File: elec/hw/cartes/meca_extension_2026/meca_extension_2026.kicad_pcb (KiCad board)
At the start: 2 copper layers, 112.5 x 54.9 mm, 168 parts, among them J1 2-1445055-3, J10 22053051, J11 22272021, J12 22272021, J13 22053051, J14 22272031, J15 22272031, J2 22272021, J20 5264-3P, J21 5264-3P, J22 5264-3P, J23 5264-3P, J24 22053031, J25 22053031, J26 22053051, J27 22053041, J28 22053031, J29 22053031, J3 22272021, J4 22053051, J5 22272021, J6 22272021, J7 22053051, J8 22272021, J9 22272021, Q1 SI2310, Q10 SI2310, Q11 SI2310, Q12 2N7002, Q19 BSS84, Q2 SI2310, Q20 2N7002, Q3 2N7002, Q4 SI2310, Q5 SI2310, Q6 2N7002, Q7 SI2310, Q8 SI2310, Q9 2N7002, U1 TCA9548APWR, U11 LV14340DDAR, U2 PCA9535PW, U3 TLA2528IRTER, U4 TLV9061IDBVR, U5 TLV9061IDBVR, U6 TLV9061IDBVR, U7 TLV9061IDBVR, U8 74HCT238PW

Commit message: meca ext : first draft of compenent placement
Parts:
- C27, C29, C30, C31, D13, J21, J22, J23, Q19, Q20, R71, R72, R73, R74, R75: moved to B.Cu
- moved C27 248.8 mm to (110.5, 102.0), turned to 90 degrees
- moved J23 240.2 mm to (59.2, 110.8), turned to 90 degrees
- moved J21 213.1 mm to (70.8, 56.1), turned to 90 degrees
- moved Q10 211.6 mm to (37.2, 103.9), turned to -90 degrees
- moved R47 207.6 mm to (37.2, 100.9), turned to 0 degrees
- moved J13 206.9 mm to (46.7, 110.8)
- moved R50 206.6 mm to (42.6, 107.8), turned to 0 degrees
- moved J22 203.4 mm to (136.5, 41.6), turned to -90 degrees
- moved R52 200.6 mm to (42.6, 105.8), turned to 0 degrees
- moved R51 200.3 mm to (46.6, 105.3), turned to -90 degrees
- moved J11 200.2 mm to (36.7, 112.9), turned to -90 degrees
- moved Q12 198.9 mm to (49.7, 105.4), turned to -90 degrees
- moved R40 192.2 mm to (161.5, 85.2), turned to 90 degrees
- moved D7 189.2 mm to (36.7, 107.4), turned to 0 degrees
- moved Q8 189.1 mm to (164.6, 85.2), turned to 0 degrees
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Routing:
- net +BATT: track 5.66 -> 22.6 mm
- net Net-(D3-A): track 0.00 -> 8.50 mm
- net Net-(D5-A): track 0.00 -> 8.50 mm
- net Net-(D7-A): track 0.00 -> 8.50 mm
- net GND: track 1.95 -> 7.78 mm
- net /solenoid_valve_cmd_1_3v3: track 0.00 -> 1.95 mm
- net /solenoid_valve_cmd_3_3v3: track 0.00 -> 1.95 mm
- net /solenoid_valve_cmd_2_3v3: track 0.00 -> 1.95 mm

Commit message: meca ext : second draft of component placement
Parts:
- C23, C24, C25, C26, R76, U1, U3: moved to B.Cu
- moved R78 242.5 mm to (118.5, 86.0), turned to -90 degrees
- moved R77 242.0 mm to (118.5, 83.0), turned to -90 degrees
- moved C13 238.9 mm to (122.5, 78.5), turned to 90 degrees
- moved R83 238.6 mm to (152.6, 90.5), turned to 0 degrees
- moved R84 234.2 mm to (152.6, 88.5), turned to 0 degrees
- moved C18 233.3 mm to (149.6, 92.0), turned to -90 degrees
- moved C25 233.1 mm to (77.0, 100.5), turned to -45 degrees
- moved C16 231.1 mm to (143.1, 81.0), turned to 90 degrees
- moved C19 230.8 mm to (147.1, 92.0), turned to -90 degrees
- moved R85 229.9 mm to (152.6, 86.5), turned to 0 degrees
- moved C17 229.3 mm to (149.6, 84.5), turned to 90 degrees
- moved R79 227.8 mm to (127.1, 76.0), turned to 0 degrees
- moved C24 227.4 mm to (143.0, 61.5), turned to 150 degrees
- moved R80 227.3 mm to (127.1, 78.0), turned to 0 degrees
- moved C15 225.8 mm to (129.6, 88.0), turned to 0 degrees
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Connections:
- net /vaccum_1/led_cmd renamed /channel_0/led_cmd
- net /vaccum_2/led_cmd renamed /channel_1/led_cmd
- net /vaccum_3/led_cmd renamed /channel_2/led_cmd
- net /vaccum_4/led_cmd renamed /channel_3/led_cmd
- R19 pad 2: Net-(U1-SC6) -> Net-(U1-SD6)
- R21 pad 2: Net-(U1-SC6) -> Net-(U1-SD7)
- R22 pad 2: Net-(U1-SC6) -> Net-(U1-SC7)
- TP1 pad 1: Net-(U1-SC6) -> Net-(U1-SD6)
- TP3 pad 1: Net-(U1-SC6) -> Net-(U1-SD7)
- TP4 pad 1: Net-(U1-SC6) -> Net-(U1-SC7)
- U1 pad 17: Net-(U1-SC6) -> Net-(U1-SD6)
- U1 pad 19: Net-(U1-SC6) -> Net-(U1-SD7)
- U1 pad 20: Net-(U1-SC6) -> Net-(U1-SC7)
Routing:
- net +BATT: track 22.6 -> 11.3 mm
- net Net-(D3-A): track 8.50 -> 0.00 mm
- net Net-(D5-A): track 8.50 -> 0.00 mm

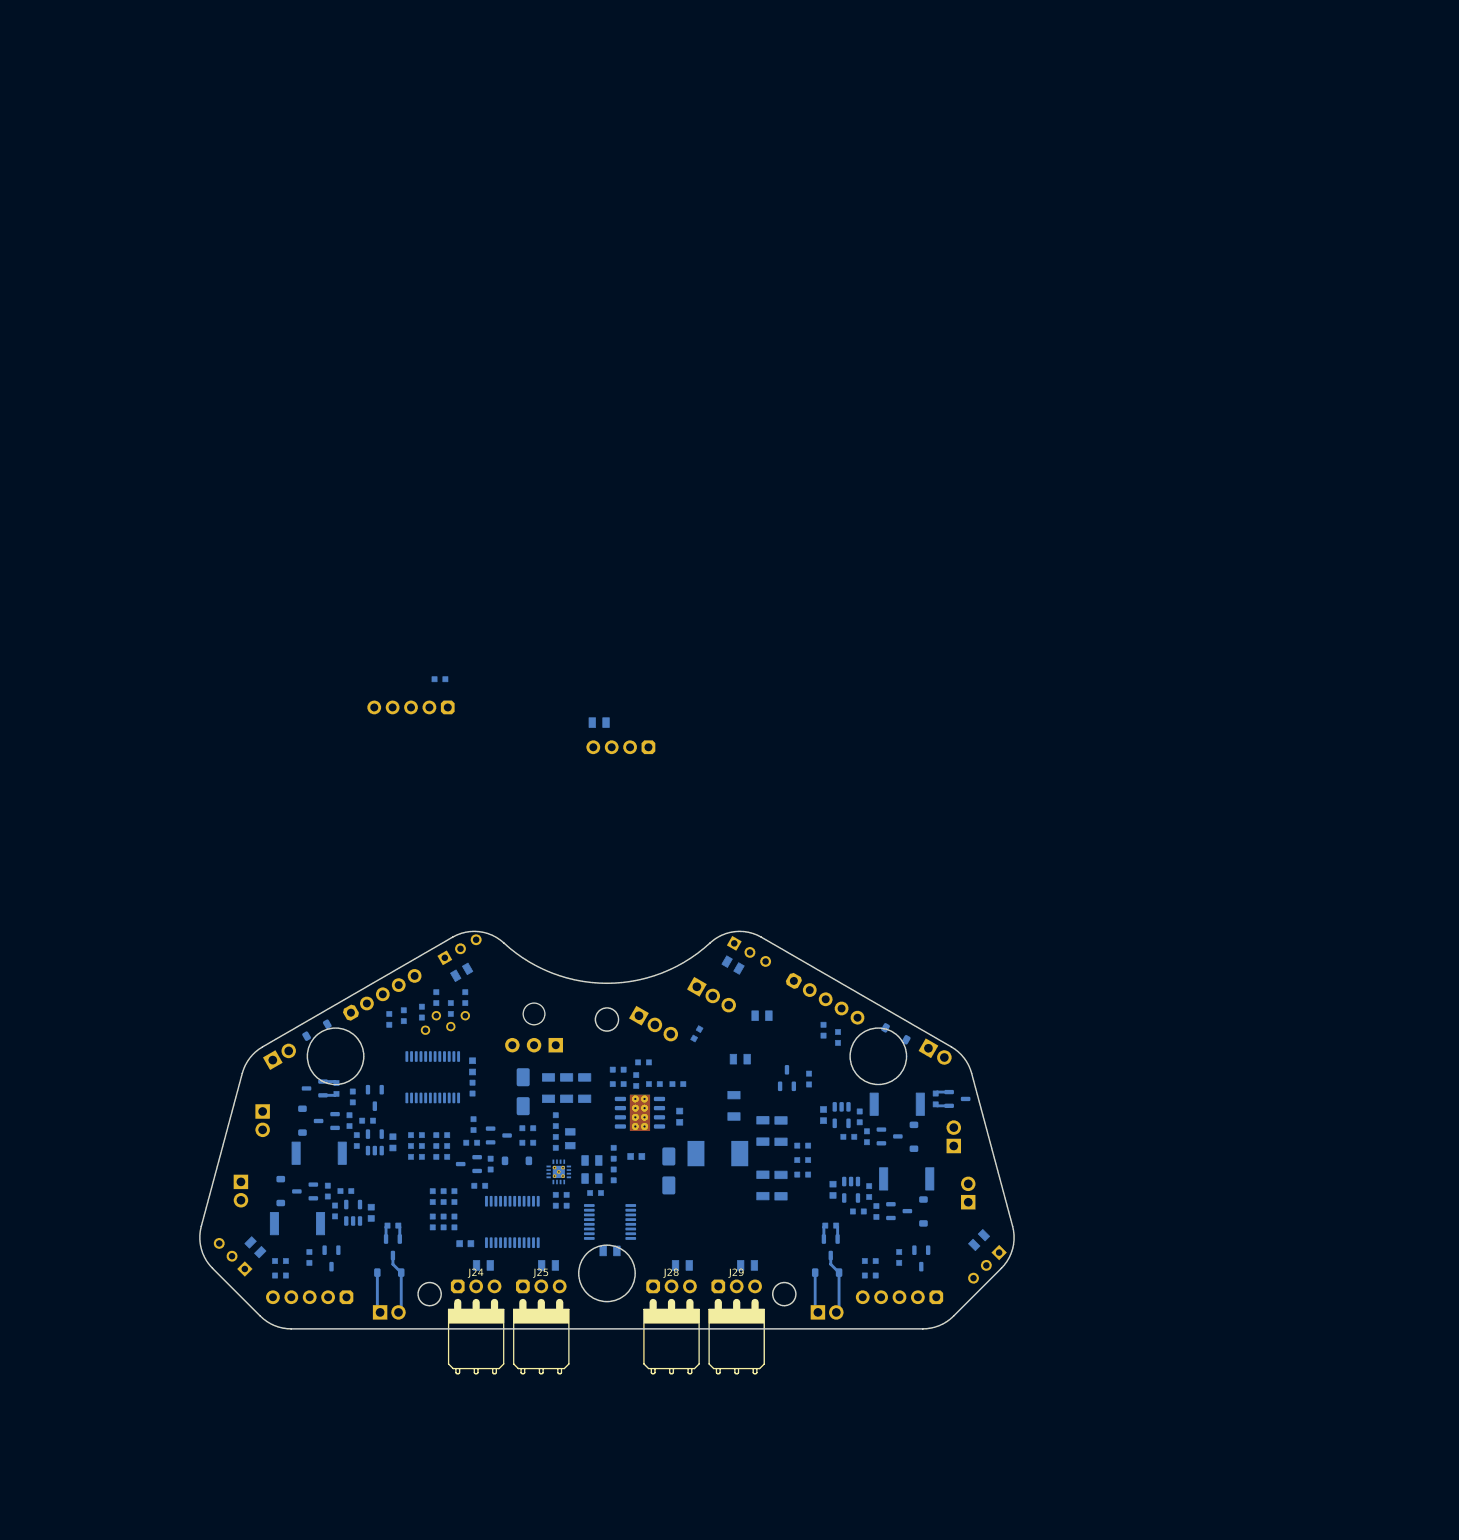
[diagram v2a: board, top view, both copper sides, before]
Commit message: meca_extension : updated board edge cut and connector placement
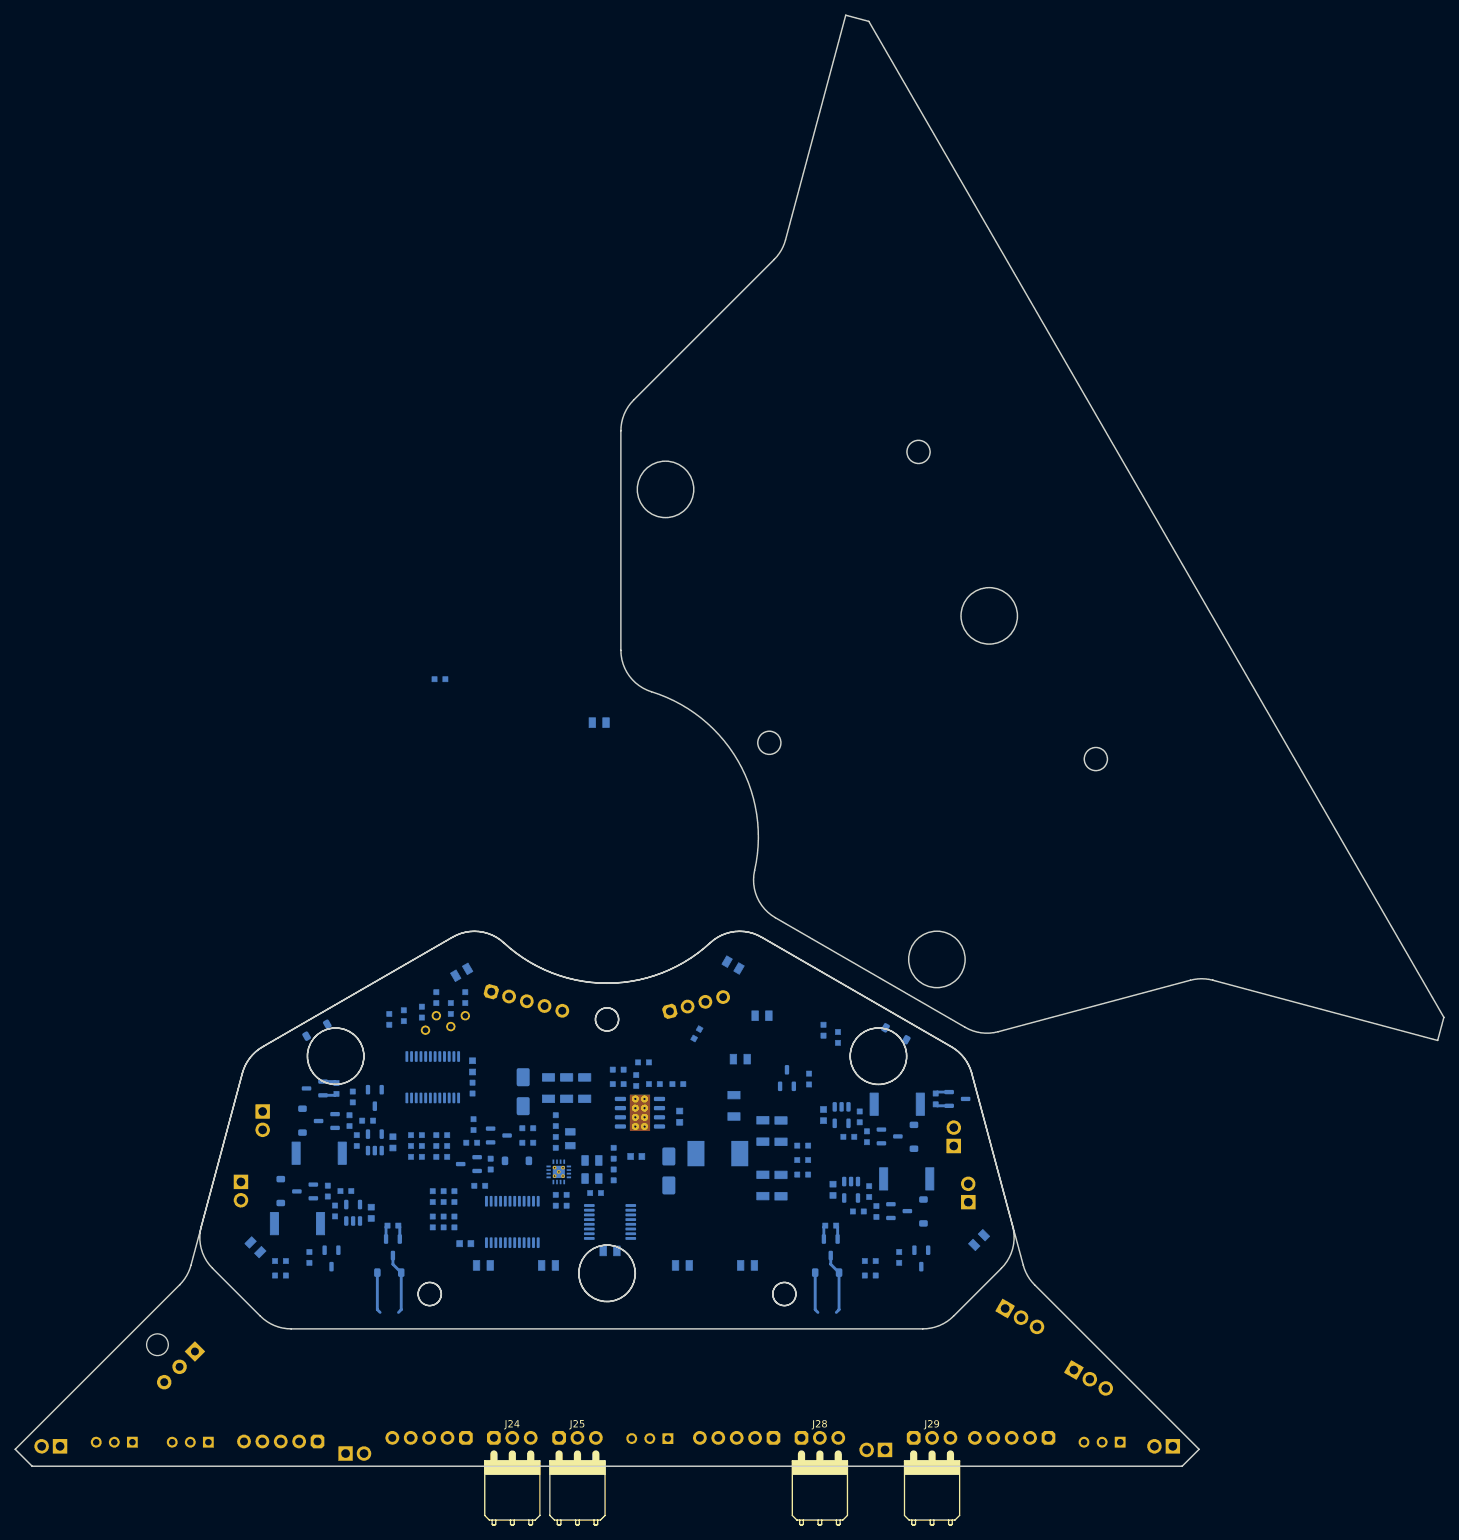
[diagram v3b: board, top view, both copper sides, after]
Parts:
- moved J22 102.8 mm to (68.0, 127.4), turned to 90 degrees
- moved J5 98.7 mm to (162.7, 128.5), turned to 90 degrees
- moved J8 97.6 mm to (90.7, 129.0), turned to -90 degrees
- moved J10 81.7 mm to (101.0, 126.8), turned to 180 degrees
- moved J7 78.4 mm to (143.5, 126.8), turned to 180 degrees
- moved J15 74.3 mm to (192.3, 118.7)
- moved J21 72.6 mm to (131.5, 126.9), turned to 90 degrees
- moved J1 66.1 mm to (66.5, 117.0), turned to 45 degrees
- moved J14 64.8 mm to (182.8, 110.2)
- moved J11 50.3 mm to (48.7, 128.0), turned to 90 degrees
- moved J2 50.0 mm to (202.5, 128.0), turned to 90 degrees
- moved J26 43.6 mm to (114.5, 66.5), turned to -15 degrees
- moved J27 37.0 mm to (137.9, 66.9), turned to 15 degrees
- moved J29 34.2 mm to (170.5, 126.8)
- moved J23 30.4 mm to (57.5, 127.4), turned to 90 degrees
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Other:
- board size 112.5 x 54.9 mm -> 197.4 x 200.5 mm

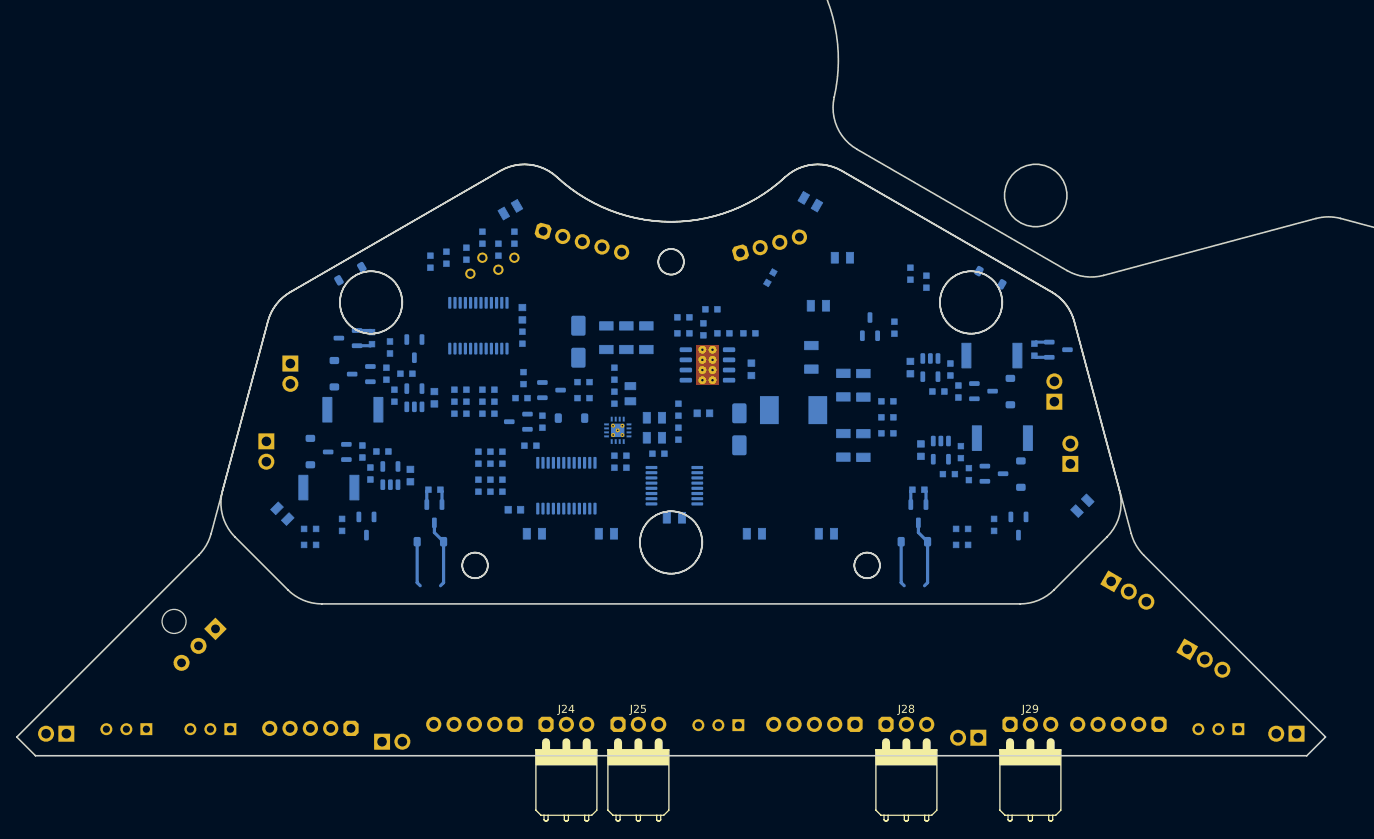
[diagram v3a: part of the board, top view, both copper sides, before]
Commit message: meca_extension : connectors placement modified
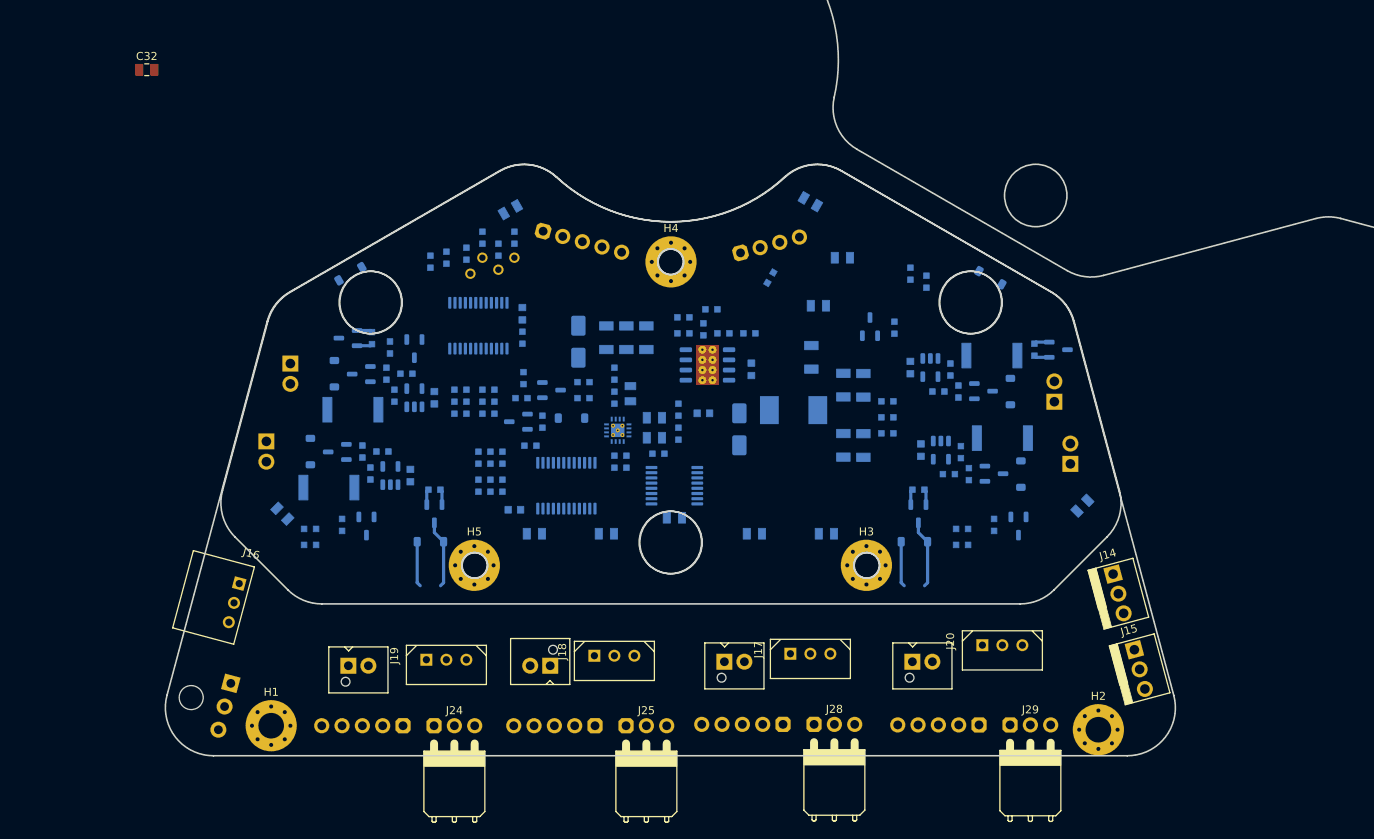
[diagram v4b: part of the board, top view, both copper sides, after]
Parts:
- removed J21, J22, J23: 5264-3P, cocotter_connectors:5264-3P
- added C32: 1µF 50V, cocotter_capacitors:C_0805_2012Metric, F.Cu at (60.0, 45.0)
- added H1: MountingHole_Pad_M3, cocotter_others:MountingHole_3.2mm_M3_Pad_Via, F.Cu at (75.6, 127.0)
- added H2: MountingHole_Pad_M3, cocotter_others:MountingHole_3.2mm_M3_Pad_Via, F.Cu at (179.0, 127.5)
- added H3: MountingHole_Pad_M3, cocotter_others:MountingHole_3.2mm_M3_Pad_Via, F.Cu at (150.0, 107.0)
- added H4: MountingHole_Pad_M3, cocotter_others:MountingHole_3.2mm_M3_Pad_Via, F.Cu at (125.6, 69.0)
- added H5: MountingHole_Pad_M3, cocotter_others:MountingHole_3.2mm_M3_Pad_Via, F.Cu at (101.0, 107.0)
- added J16: 5264-3P, cocotter_connectors:5264-3P, F.Cu at (71.0, 111.6)
- added J17: 5267-3P, cocotter_connectors:5267-3P, F.Cu at (143.0, 118.0)
- added J18: 5267-3P, cocotter_connectors:5267-3P, F.Cu at (118.5, 118.2)
- added J19: 5267-3P, cocotter_connectors:5267-3P, F.Cu at (97.5, 118.8)
- J11, J2, J5, J8: value 22272021 -> B2B-XH-A; footprint cocotter_connectors:22272021 -> cocotter_connectors:B2B-XH-A; moved to F.Cu
- J14, J15: moved to F.Cu
- J20: value 5264-3P -> 5267-3P; footprint cocotter_connectors:5264-3P -> cocotter_connectors:5267-3P; moved to F.Cu
- moved J2 46.4 mm to (157.0, 119.0)
- moved J11 38.7 mm to (86.5, 119.5)
- moved J5 30.7 mm to (133.5, 119.0)
- moved J20 29.0 mm to (167.0, 116.9)
- moved J4 22.5 mm to (159.0, 126.9)
- moved J8 20.8 mm to (109.2, 119.5)
- moved J24 14.0 mm to (98.5, 127.0)
- moved J10 10.0 mm to (111.0, 127.0)
- moved J28 9.00 mm to (146.0, 126.8)
- moved J7 9.00 mm to (134.5, 126.8)
- moved J1 8.26 mm to (69.8, 124.6), turned to 75 degrees
- moved J15 8.23 mm to (184.2, 120.0), turned to 15 degrees
- moved J13 6.51 mm to (87.0, 127.0)
- moved J14 1.33 mm to (181.5, 110.5), turned to 15 degrees
- moved J25 1.01 mm to (122.5, 127.0)
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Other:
- board size 197.4 x 200.5 mm -> 178.8 x 200.5 mm
- board text added: "trous de fixation a replacer correctement, je les ai juste jetés"
